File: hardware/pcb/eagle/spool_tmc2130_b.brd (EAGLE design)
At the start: 50 x 90 mm, 29 parts, among them J1 PINHD-1X8, J2 F-1X08-SIP-100-40, J3 F-1X02-SIP-100-32, K1 G6K-2P-Y, U1 NJM7805SDL, U2 ATTINY85-20PU, X1 JST-XH-02-PIN-LONG-PAD, X2 JST-XH-04-PIN-LONG-PAD, X3 JST-XH-02-PIN-LONG-PAD, X4 JST-XH-02-PIN-LONG-PAD, X5 JST-XH-02-PIN-LONG-PAD, X6 JST-XH-02-PIN-LONG-PAD, X9 JST-XH-03-PIN-LONG-PAD

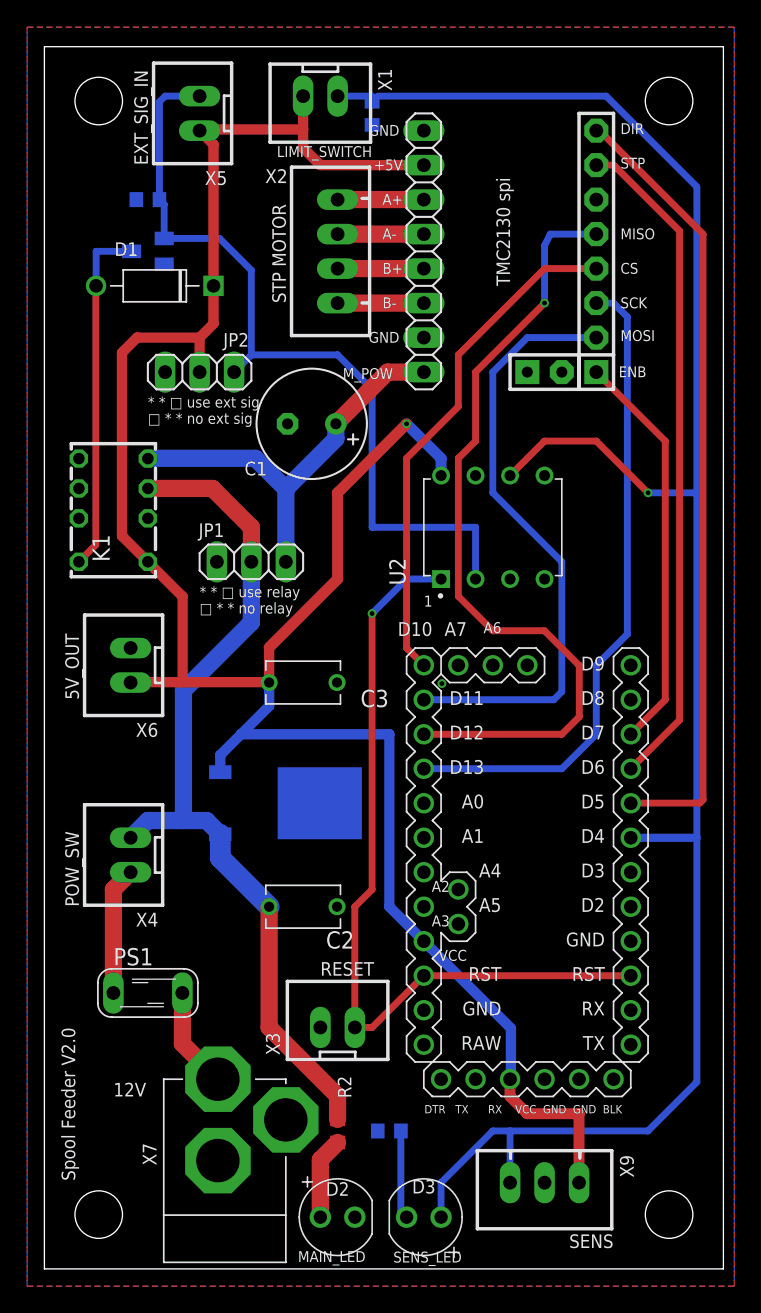
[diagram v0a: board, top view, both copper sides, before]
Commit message: Control board rev.B: EAGLE files, schematic PDF, BOM and docs
The board was revised in Autodesk Fusion and exported in EAGLE 9.7.0
format. rev.A (as built) is kept in tag pcb-rev.A.

- EXT_SENSE: X5 pin 2 and JP2 pin 1 to ATtiny85 PB4 through R6 10k,
  pull-down R5 10k
- T1 DTC123JKA, R2 2.2k, D3 driven from Pro Mini D8 with R4 470
- Chip resistors 0603 -> 0805
- Schematic and board netlists identical (26 nets); connectivity of
  all nets checked on the Gerber output of the CAM processor
- Schematic PDF (A3) added
- BOM, wiring, README, LICENSE (Autodesk Resistor library) and
  CHANGELOG updated

Co-Authored-By: Claude Opus 5.5 <noreply@anthropic.com>
Claude-Session: https://claude.ai/code/session_01CN5z7kNkBV6zKj8DLApdnx
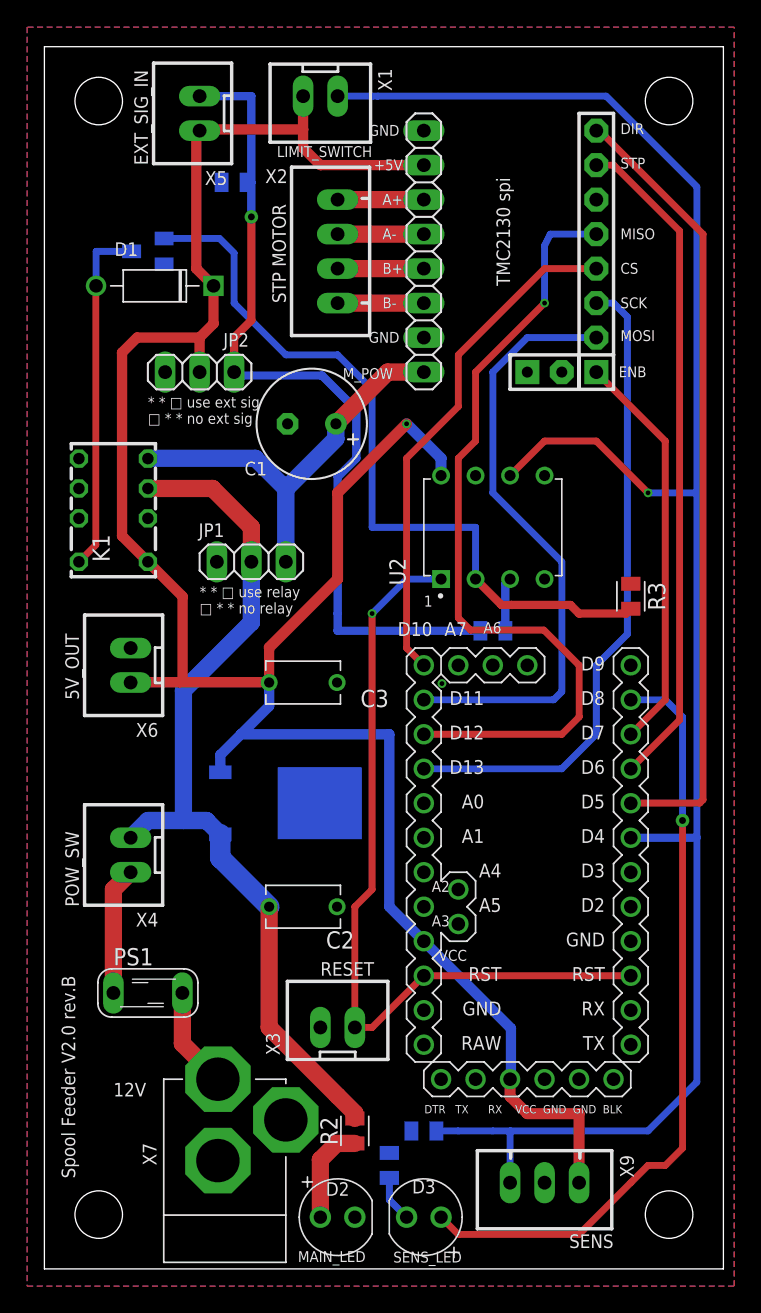
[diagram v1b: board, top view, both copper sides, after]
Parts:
- added R5, R6: 10k, Resistor:RESC2012X65
- C1: value (none) -> 100uF
- C2: value RDER73A103K2K1H03B -> 0.33uF
- C3: value RDER73A103K2K1H03B -> 0.1uF
- PS1: value (none) -> RXEF135
- R1, R3: device resistor:R0603 -> Resistor:RESC2012X65
- R2: value 680 -> 2.2k; device resistor:R0603 -> Resistor:RESC2012X65
- R4: value 150 -> 470; device resistor:R0603 -> Resistor:RESC2012X65
- T1: value (none) -> DTC123JKA
- moved R1 75.0 mm to (27.9, 10.2), turned to 180 degrees
- moved R3 46.0 mm to (43.2, 49.5), flipped to the top, turned to 270 degrees
- moved R4 2.54 mm to (25.4, 7.62), turned to 270 degrees
- moved R2 1.27 mm to (22.9, 10.2)
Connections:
- new net D8_LED: ARDUINO1.D8, D3.1
- new net EXT_SENSE: JP2.1, R5.2, R6.1, X5.2
- new net N$1: R6.2, U2.3
- net D4: no longer D3.1
- net EXT_IN: no longer JP2.1, X5.2
- net GND: now also R5.1
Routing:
- net EXT_SENSE: track 0.00 -> 62.5 mm, vias 0 -> 1
- net D8_LED: track 0.00 -> 57.0 mm, vias 0 -> 1
- net D4: track 145.2 -> 140.9 mm
- net EXT_IN: track 60.3 -> 56.3 mm
- net N$1: track 0.00 -> 3.96 mm
- net N$2: track 6.52 -> 3.42 mm
- net N$16: track 6.03 -> 7.27 mm
- net D12-MISO: track 59.6 -> 60.5 mm
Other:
- board text added: "Spool Feeder V2.0 rev.B"
- board text removed: "Spool Feeder V2.0"
